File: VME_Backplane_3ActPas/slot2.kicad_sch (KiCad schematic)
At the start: 7 parts, among them X101 DIN41612_03x32_ABC_VMEbus, X402A1 Jumper_2_Open, X402B1 Jumper_2_Open, X402C1 Jumper_2_Open, X402D1 Jumper_2_Open, X502 Jumper_2_Open

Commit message: Rename sheets to reflect their slots
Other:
- title: SOCKET 1 -> SLOT 2
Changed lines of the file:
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@@
   (paper "A4")
   (title_block
-    (title "SOCKET 1")
-    (date "2023-10-10")
+    (title "SLOT 2")
+    (date "2024-01-02")
     (rev "1")
     (company "(C) TOM STOREY")
@@
   (symbol (lib_id "power:+5V") (at 55.88 149.86 0) (unit 1)
     (in_bom yes) (on_board yes) (fields_autoplaced)
-    (property "Reference" "#PWR0118" (id 0) (at 55.88 153.67 0)
+    (property "Reference" "#PWR?" (id 0) (at 55.88 153.67 0)
       (effects (font (size 1.27 1.27)) hide)
     )
@@
   (symbol (lib_id "power:-12V") (at 55.88 177.8 180) (unit 1)
     (in_bom yes) (on_board yes) (fields_autoplaced)
-    (property "Reference" "#PWR0122" (id 0) (at 55.88 180.34 0)
+    (property "Reference" "#PWR?" (id 0) (at 55.88 180.34 0)
       (effects (font (size 1.27 1.27)) hide)
     )
@@
   (symbol (lib_id "power:+BATT") (at 55.88 124.46 0) (unit 1)
     (in_bom yes) (on_board yes) (fields_autoplaced)
-    (property "Reference" "#PWR0119" (id 0) (at 55.88 128.27 0)
+    (property "Reference" "#PWR?" (id 0) (at 55.88 128.27 0)
       (effects (font (size 1.27 1.27)) hide)
     )
@@
   (symbol (lib_id "power:GND") (at 55.88 165.1 0) (unit 1)
     (in_bom yes) (on_board yes) (fields_autoplaced)
-    (property "Reference" "#PWR0121" (id 0) (at 55.88 171.45 0)
+    (property "Reference" "#PWR?" (id 0) (at 55.88 171.45 0)
       (effects (font (size 1.27 1.27)) hide)
     )
@@
   (symbol (lib_id "power:+12V") (at 55.88 137.16 0) (unit 1)
     (in_bom yes) (on_board yes) (fields_autoplaced)
-    (property "Reference" "#PWR0120" (id 0) (at 55.88 140.97 0)
-      (effects (font (size 1.27 1.27)) hide)
-    )
+    (property "Reference" "#PWR?" (id 0) (at 55.88 140.97 0)
+      (effects (font (size 1.27 1.27)) hide)
+    )

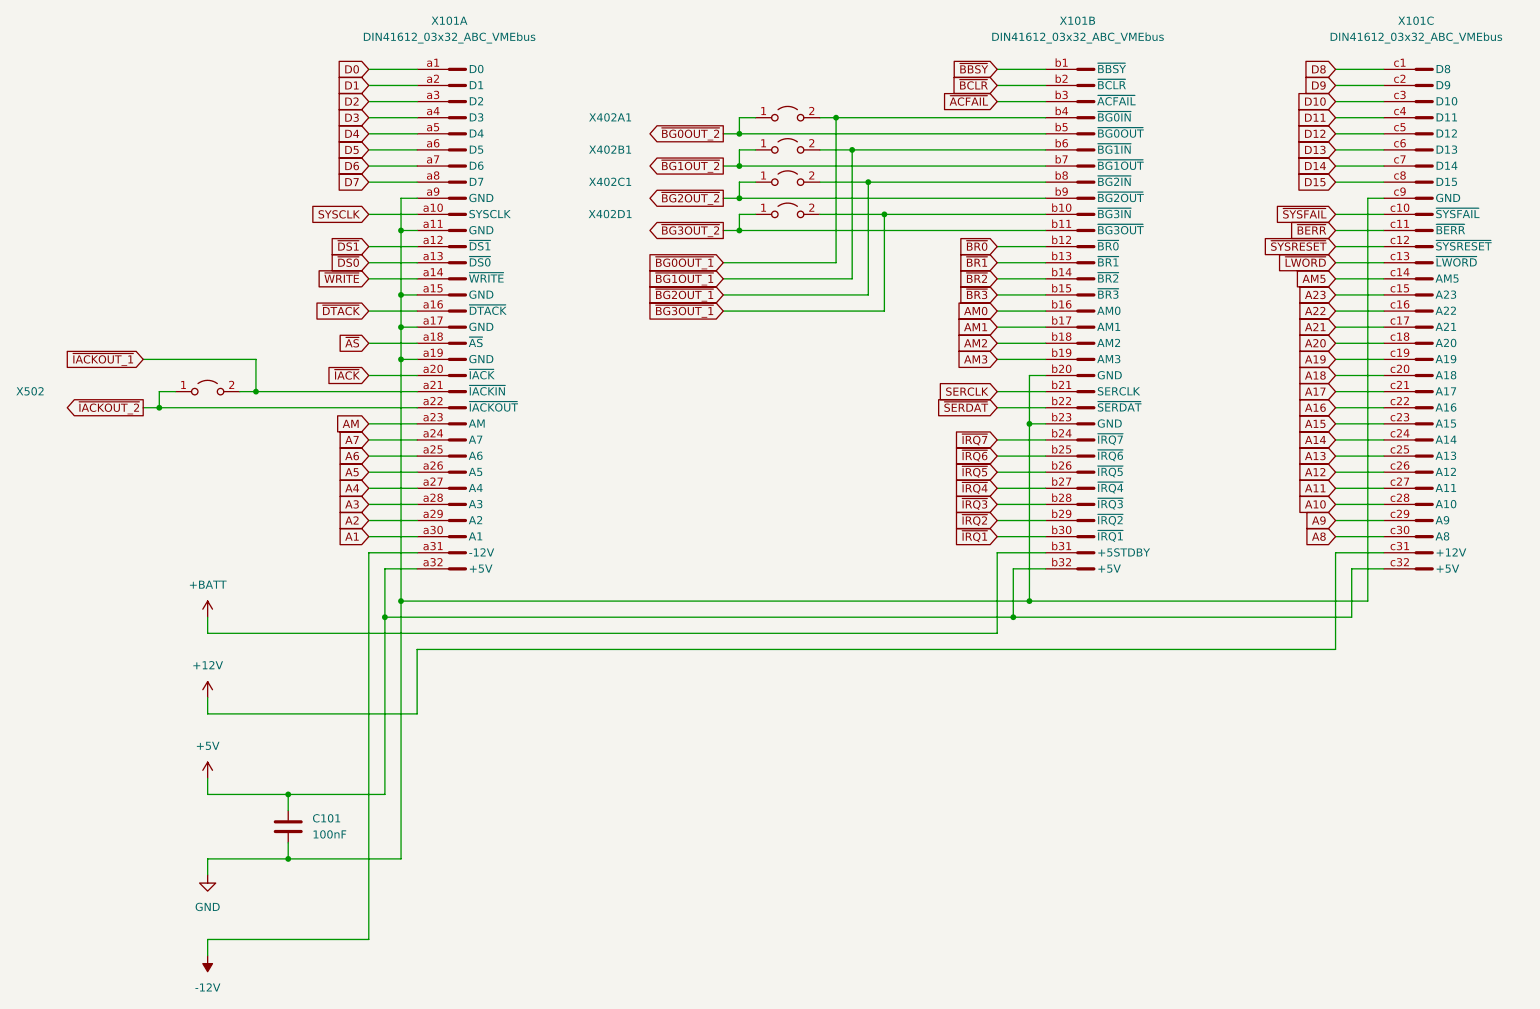
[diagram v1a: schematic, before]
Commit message: Change to own DIN 41612 footprint with 3D model
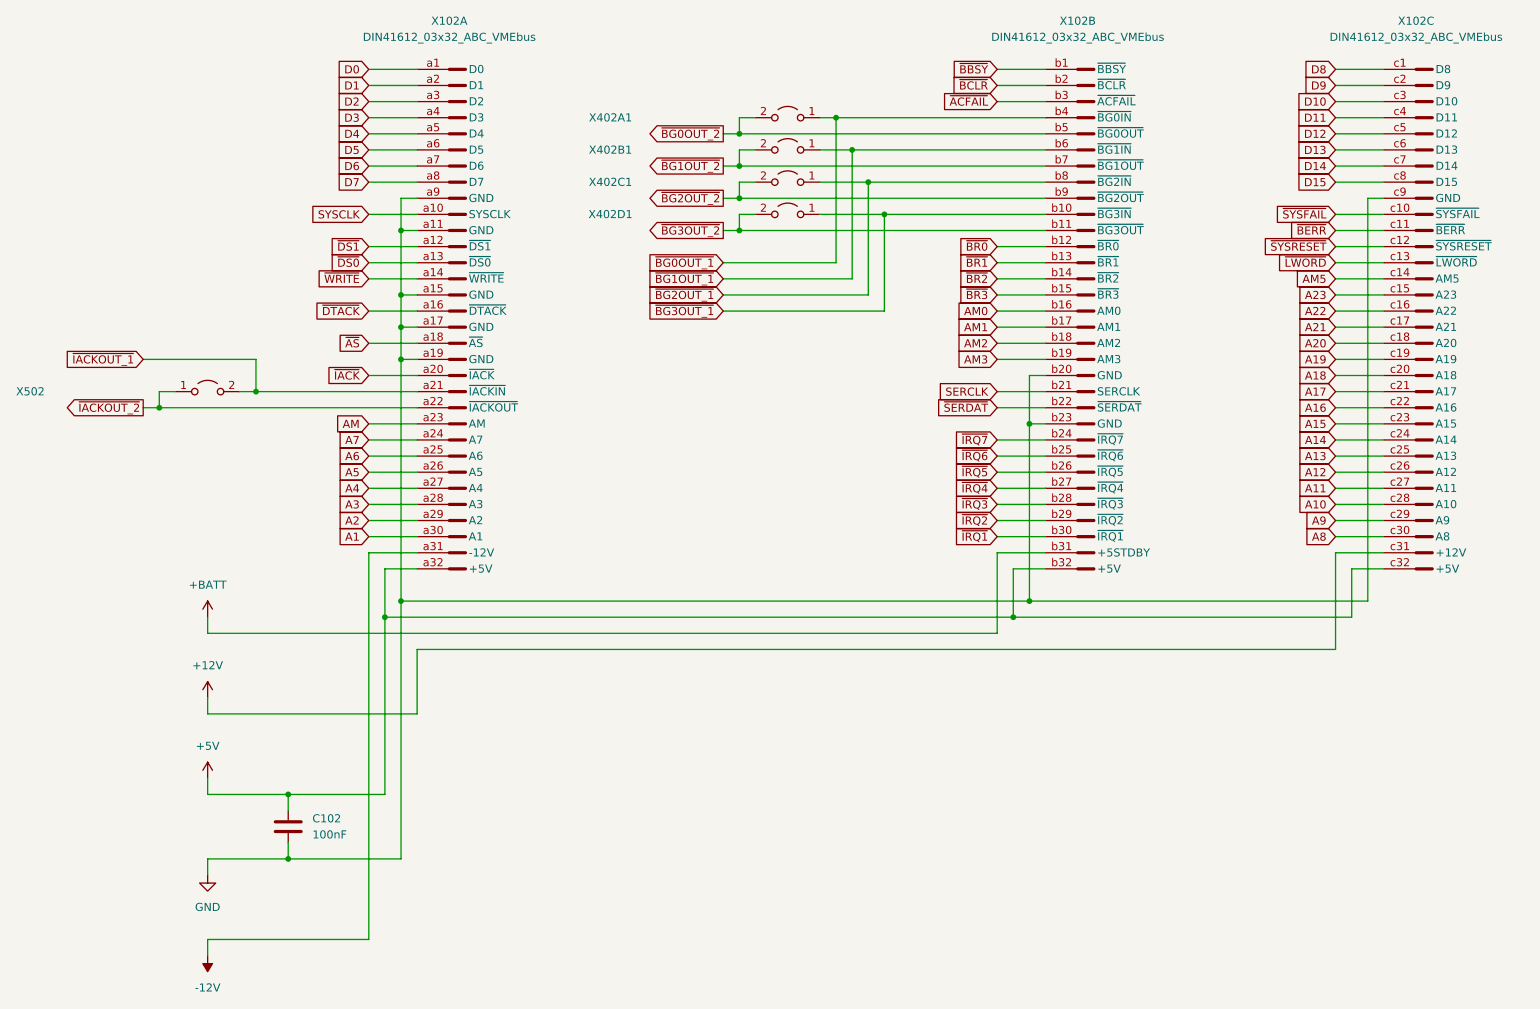
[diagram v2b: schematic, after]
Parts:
- X102: renamed from X101; footprint Connector_DIN:DIN41612_C_3x32_Female_Vertical_THT -> COMET footprints:Connector_DIN41612_C_3x32_Female_Vertical_THT
- X102: renamed from X101; footprint Connector_DIN:DIN41612_C_3x32_Male_Horizontal_THT -> COMET footprints:Connector_DIN41612_C_3x32_Female_Vertical_THT
- renumbered C101 to C102
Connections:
- net ~{BG0OUT_1}: now also X402A1.1 (A); no longer X402A1.2 (B)
- net ~{BG0OUT_2}: now also X402A1.2 (B); no longer X402A1.1 (A)
- net ~{BG1OUT_1}: now also X402B1.1 (A); no longer X402B1.2 (B)
- net ~{BG1OUT_2}: now also X402B1.2 (B); no longer X402B1.1 (A)
- net ~{BG2OUT_1}: now also X402C1.1 (A); no longer X402C1.2 (B)
- net ~{BG2OUT_2}: now also X402C1.2 (B); no longer X402C1.1 (A)
- net ~{BG3OUT_1}: now also X402D1.1 (A); no longer X402D1.2 (B)
- net ~{BG3OUT_2}: now also X402D1.2 (B); no longer X402D1.1 (A)
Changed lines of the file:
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@@
     )
   )
-  (symbol (lib_id "Jumper:Jumper_2_Open") (at 147.32 60.96 0) (unit 1)
+  (symbol (lib_id "Jumper:Jumper_2_Open") (at 147.32 60.96 0) (mirror y) (unit 1)
     (in_bom yes) (on_board yes)
     (property "Reference" "X402D1" (id 0) (at 119.38 60.96 0))
@@
     (pin "2")
   )
-  (symbol (lib_id "Jumper:Jumper_2_Open") (at 147.32 55.88 0) (unit 1)
+  (symbol (lib_id "Jumper:Jumper_2_Open") (at 147.32 55.88 0) (mirror y) (unit 1)
     (in_bom yes) (on_board yes)
     (property "Reference" "X402C1" (id 0) (at 119.38 55.88 0))
@@
   (symbol (lib_id "power:+5V") (at 55.88 149.86 0) (unit 1)
     (in_bom yes) (on_board yes) (fields_autoplaced)
-    (property "Reference" "#PWR?" (id 0) (at 55.88 153.67 0)
+    (property "Reference" "#PWR0128" (id 0) (at 55.88 153.67 0)
       (effects (font (size 1.27 1.27)) hide)
     )
@@
     (pin "1")
   )
-  (symbol (lib_id "Jumper:Jumper_2_Open") (at 147.32 50.8 0) (unit 1)
+  (symbol (lib_id "Jumper:Jumper_2_Open") (at 147.32 50.8 0) (mirror y) (unit 1)
     (in_bom yes) (on_board yes)
     (property "Reference" "X402B1" (id 0) (at 119.38 50.8 0))
@@
   (symbol (lib_id "power:-12V") (at 55.88 177.8 180) (unit 1)
     (in_bom yes) (on_board yes) (fields_autoplaced)
-    (property "Reference" "#PWR?" (id 0) (at 55.88 180.34 0)
+    (property "Reference" "#PWR0126" (id 0) (at 55.88 180.34 0)
       (effects (font (size 1.27 1.27)) hide)
     )
@@
   (symbol (lib_id "power:+BATT") (at 55.88 124.46 0) (unit 1)
     (in_bom yes) (on_board yes) (fields_autoplaced)
-    (property "Reference" "#PWR?" (id 0) (at 55.88 128.27 0)
+    (property "Reference" "#PWR0129" (id 0) (at 55.88 128.27 0)
       (effects (font (size 1.27 1.27)) hide)
     )
@@
   (symbol (lib_id "power:GND") (at 55.88 165.1 0) (unit 1)
     (in_bom yes) (on_board yes) (fields_autoplaced)
-    (property "Reference" "#PWR?" (id 0) (at 55.88 171.45 0)
+    (property "Reference" "#PWR0127" (id 0) (at 55.88 171.45 0)
       (effects (font (size 1.27 1.27)) hide)
     )
@@
     (pin "1")
   )
-  (symbol (lib_id "Jumper:Jumper_2_Open") (at 147.32 45.72 0) (unit 1)
+  (symbol (lib_id "Jumper:Jumper_2_Open") (at 147.32 45.72 0) (mirror y) (unit 1)
     (in_bom yes) (on_board yes)
     (property "Reference" "X402A1" (id 0) (at 119.38 45.72 0))
@@
   (symbol (lib_id "COMET symbols:C") (at 68.58 157.48 0) (unit 1)
     (in_bom yes) (on_board yes) (fields_autoplaced)
-    (property "Reference" "C101" (id 0) (at 72.39 156.2099 0)
+    (property "Reference" "C102" (id 0) (at 72.39 156.2099 0)
       (effects (font (size 1.27 1.27)) (justify left))
     )
@@
   (symbol (lib_id "COMET symbols:DIN41612_03x32_ABC_VMEbus") (at 93.98 76.2 0) (unit 1)
     (in_bom yes) (on_board yes)
-    (property "Reference" "X101" (id 0) (at 93.98 30.48 0))
+    (property "Reference" "X102" (id 0) (at 93.98 30.48 0))
     (property "Value" "DIN41612_03x32_ABC_VMEbus" (id 1) (at 93.98 33.02 0))
-    (property "Footprint" "Connector_DIN:DIN41612_C_3x32_Female_Vertical_THT" (id 2) (at 96.52 76.2 0)
+    (property "Footprint" "COMET footprints:Connector_DIN41612_C_3x32_Female_Vertical_THT" (id 2) (at 96.52 76.2 0)
       (effects (font (size 1.27 1.27)) hide)
     )
@@
   (symbol (lib_id "COMET symbols:DIN41612_03x32_ABC_VMEbus") (at 246.38 76.2 0) (unit 3)
     (in_bom yes) (on_board yes)
-    (property "Reference" "X101" (id 0) (at 246.38 30.48 0))
+    (property "Reference" "X102" (id 0) (at 246.38 30.48 0))
     (property "Value" "DIN41612_03x32_ABC_VMEbus" (id 1) (at 246.38 33.02 0))
-    (property "Footprint" "Connector_DIN:DIN41612_C_3x32_Male_Horizontal_THT" (id 2) (at 248.92 76.2 0)
+    (property "Footprint" "COMET footprints:Connector_DIN41612_C_3x32_Female_Vertical_THT" (id 2) (at 248.92 76.2 0)
       (effects (font (size 1.27 1.27)) hide)
     )
@@
   (symbol (lib_id "power:+12V") (at 55.88 137.16 0) (unit 1)
     (in_bom yes) (on_board yes) (fields_autoplaced)
-    (property "Reference" "#PWR?" (id 0) (at 55.88 140.97 0)
+    (property "Reference" "#PWR0130" (id 0) (at 55.88 140.97 0)
       (effects (font (size 1.27 1.27)) hide)
     )
@@
   (symbol (lib_id "COMET symbols:DIN41612_03x32_ABC_VMEbus") (at 193.04 76.2 0) (unit 2)
     (in_bom yes) (on_board yes)
-    (property "Reference" "X101" (id 0) (at 193.04 30.48 0))
+    (property "Reference" "X102" (id 0) (at 193.04 30.48 0))
     (property "Value" "DIN41612_03x32_ABC_VMEbus" (id 1) (at 193.04 33.02 0))
-    (property "Footprint" "Connector_DIN:DIN41612_C_3x32_Male_Horizontal_THT" (id 2) (at 195.58 76.2 0)
-      (effects (font (size 1.27 1.27)) hide)
-    )
+    (property "Footprint" "COMET footprints:Connector_DIN41612_C_3x32_Female_Vertical_THT" (id 2) (at 195.58 76.2 0)
+      (effects (font (size 1.27 1.27)) hide)
+    )

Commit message: Add/update revision information in schematics and PCB
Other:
- company: (C) TOM STOREY -> TOM STOREY
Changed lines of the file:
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@@
   (title_block
     (title "SLOT 2")
-    (date "2024-01-02")
+    (date "2024-01-03")
     (rev "1")
-    (company "(C) TOM STOREY")
+    (company "TOM STOREY")
     (comment 1 "FREE FOR NON-COMMERCIAL USE")
   )
